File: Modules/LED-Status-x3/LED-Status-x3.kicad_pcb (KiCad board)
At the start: 4 copper layers, 6 parts

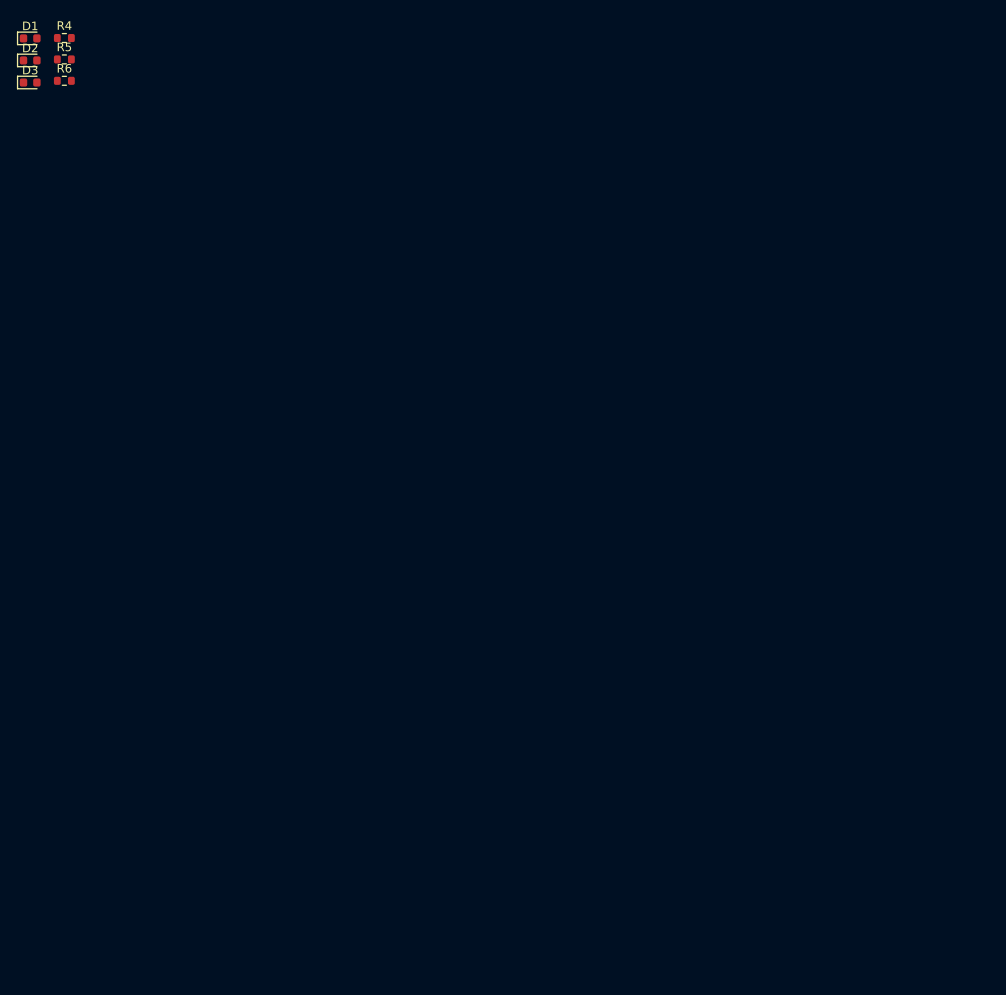
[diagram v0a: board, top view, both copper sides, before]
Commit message: Lay out the LED-Status-x3 module
14 x 11 mm, 4 layers, GND on all four. Three columns at 2.6 mm pitch, LED
above its resistor. Breakout row at y 108.5: two GND vias and the three
LED nets with 1.0 mm stubs on B.Cu. Five F.Fab labels.

DRC: 0 errors, 0 unconnected, 0 parity. The 3 track_dangling warnings are
the 3 interface stubs. Canary 10 to 77.

Co-Authored-By: Claude Opus 5.5 (1M context) <noreply@anthropic.com>
Claude-Session: https://claude.ai/code/session_01ErAAfkmF4h3T5yfrw21utF
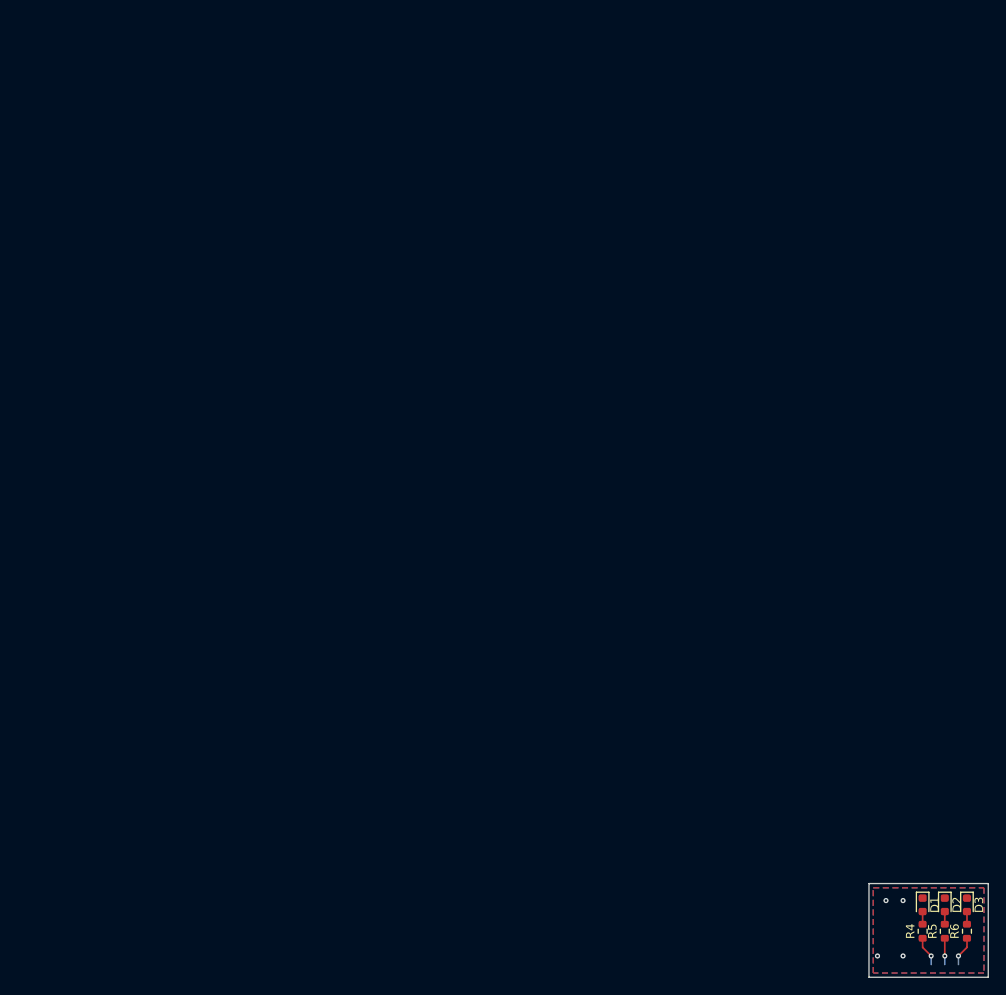
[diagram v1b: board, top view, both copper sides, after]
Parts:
- moved D3 146.3 mm to (111.5, 102.5), turned to -90 degrees
- moved D2 146.1 mm to (108.9, 102.5), turned to -90 degrees
- moved D1 146.0 mm to (106.3, 102.5), turned to -90 degrees
- moved R6 145.6 mm to (111.5, 105.6), turned to 90 degrees
- moved R5 145.4 mm to (108.9, 105.6), turned to 90 degrees
- moved R4 145.4 mm to (106.3, 105.6), turned to 90 degrees
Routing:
- net /LED_RF_TX: track 0.00 -> 3.49 mm, vias 0 -> 1
- net /LED_FAULT: track 0.00 -> 3.49 mm, vias 0 -> 1
- net /LED_LEARN: track 0.00 -> 3.08 mm, vias 0 -> 1
- net Net-(D3-A): track 0.00 -> 1.49 mm
- net Net-(D2-A): track 0.00 -> 1.49 mm
- net Net-(D1-A): track 0.00 -> 1.49 mm
- net GND: vias 0 -> 4
- added copper zone on B.Cu, net GND
- added copper zone on F.Cu, net GND
- added copper zone on In1.Cu, net GND
- added copper zone on In2.Cu, net GND
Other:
- board outline added: 14 x 11 mm
- board text added: "GND"
- board text added: "LED_FAULT"
- board text added: "LED_LEARN"
- board text added: "LED_RF_TX"

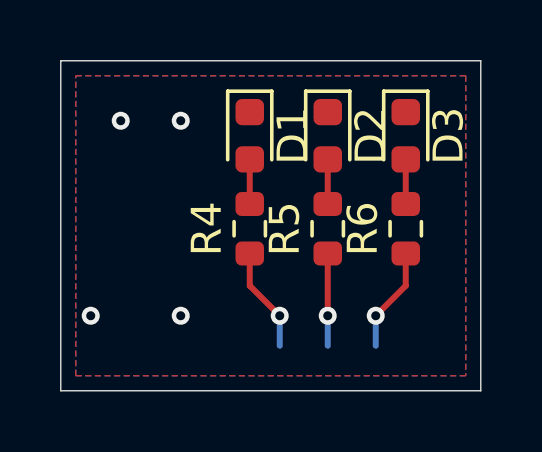
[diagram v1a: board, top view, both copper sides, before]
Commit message: Restore footprints and move passive references to F.Fab
GUI batch 2a on all eight module boards. Update Footprints from Library
restores the (units) blocks that Konnect IPC writes dropped: U10, U1, SW1,
SW2 and U4 no longer report lib_footprint_mismatch. Reference designators of
C, R, L, FB, D, Y and TP parts move to F.Fab. U, J and SW stay on the silk.

Every board: DRC 0 errors, 0 unconnected, 0 parity, the canary fires, and
track_dangling equals the interface stub count.

Co-Authored-By: Claude Opus 5.5 (1M context) <noreply@anthropic.com>
Claude-Session: https://claude.ai/code/session_01ErAAfkmF4h3T5yfrw21utF
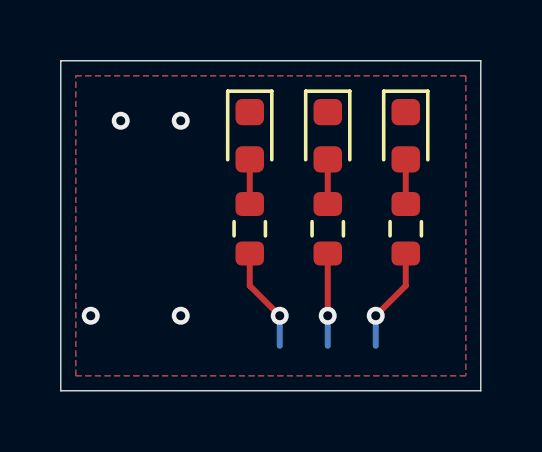
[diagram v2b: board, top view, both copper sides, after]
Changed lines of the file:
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@@
 		(tags "LED")
 		(property "Reference" "D3"
-			(at 0 -1.43 -90)
-			(layer "F.SilkS")
+			(at 0 -1.43 270)
+			(layer "F.Fab")
 			(effects
 				(font
@@
 		)
 		(property "Value" "Red 625nm 0603"
-			(at 0 1.43 -90)
+			(at 0 1.43 270)
 			(layer "F.Fab")
 			(effects
@@
 		)
 		(property "Datasheet" "https://www.we-online.com/components/products/datasheet/150060RS75000.pdf"
-			(at 0 0 -90)
+			(at 0 0 270)
 			(layer "F.Fab")
 			(hide yes)
@@
 		)
 		(property "Description" ""
-			(at 0 0 -90)
+			(at 0 0 270)
 			(layer "F.Fab")
 			(hide yes)
@@
 		)
 		(property "KiLib_Generator" "SMD_2terminal_chip_molded"
-			(at 0 0 -90)
+			(at 0 0 270)
 			(layer "F.SilkS")
 			(hide yes)
@@
 		)
 		(property "MPN" "150060RS75000"
-			(at 0 0 -90)
+			(at 0 0 270)
 			(unlocked yes)
 			(layer "F.Fab")
@@
 		)
 		(property "Manufacturer" "Wurth Elektronik"
-			(at 0 0 -90)
+			(at 0 0 270)
 			(unlocked yes)
 			(layer "F.Fab")
@@
 		)
 		(property "Sim.Pins" "1=K 2=A"
-			(at 0 0 -90)
+			(at 0 0 270)
 			(unlocked yes)
 			(layer "F.Fab")
@@
 		)
 		(fp_text user "${REFERENCE}"
-			(at 0 0 -90)
+			(at 0 0 270)
 			(layer "F.Fab")
 			(effects
@@
 		(property "Reference" "R5"
 			(at 0 -1.43 90)
-			(layer "F.SilkS")
+			(layer "F.Fab")
 			(effects
 				(font
@@
 		(tags "LED")
 		(property "Reference" "D2"
-			(at 0 -1.43 -90)
-			(layer "F.SilkS")
+			(at 0 -1.43 270)
+			(layer "F.Fab")
 			(effects
 				(font
@@
 		)
 		(property "Value" "Amber 605nm 0603"
-			(at 0 1.43 -90)
+			(at 0 1.43 270)
 			(layer "F.Fab")
 			(effects
@@
 		)
 		(property "Datasheet" "https://www.we-online.com/components/products/datasheet/150060AS75000.pdf"
-			(at 0 0 -90)
+			(at 0 0 270)
 			(layer "F.Fab")
 			(hide yes)
@@
 		)
 		(property "Description" ""
-			(at 0 0 -90)
+			(at 0 0 270)
 			(layer "F.Fab")
 			(hide yes)
@@
 		)
 		(property "KiLib_Generator" "SMD_2terminal_chip_molded"
-			(at 0 0 -90)
+			(at 0 0 270)
 			(layer "F.SilkS")
 			(hide yes)
@@
 		)
 		(property "MPN" "150060AS75000"
-			(at 0 0 -90)
+			(at 0 0 270)
 			(unlocked yes)
 			(layer "F.Fab")
@@
 		)
 		(property "Manufacturer" "Wurth Elektronik"
-			(at 0 0 -90)
+			(at 0 0 270)
 			(unlocked yes)
 			(layer "F.Fab")
@@
 		)
 		(property "Sim.Pins" "1=K 2=A"
-			(at 0 0 -90)
+			(at 0 0 270)
 			(unlocked yes)
 			(layer "F.Fab")
@@
 		)
 		(fp_text user "${REFERENCE}"
-			(at 0 0 -90)
+			(at 0 0 270)
 			(layer "F.Fab")
 			(effects
@@
 		(property "Reference" "R4"
 			(at 0 -1.43 90)
-			(layer "F.SilkS")
+			(layer "F.Fab")
 			(effects
 				(font
@@
 		(tags "LED")
 		(property "Reference" "D1"
-			(at 0 -1.43 -90)
-			(layer "F.SilkS")
+			(at 0 -1.43 270)
+			(layer "F.Fab")
 			(effects
 				(font
@@
 		)
 		(property "Value" "Green 570nm 0603"
-			(at 0 1.43 -90)
+			(at 0 1.43 270)
 			(layer "F.Fab")
 			(effects
@@
 		)
 		(property "Datasheet" "https://www.we-online.com/components/products/datasheet/150060VS75000.pdf"
-			(at 0 0 -90)
+			(at 0 0 270)
 			(layer "F.Fab")
 			(hide yes)
@@
 		)
 		(property "Description" ""
-			(at 0 0 -90)
+			(at 0 0 270)
 			(layer "F.Fab")
 			(hide yes)
@@
 		)
 		(property "KiLib_Generator" "SMD_2terminal_chip_molded"
-			(at 0 0 -90)
+			(at 0 0 270)
 			(layer "F.SilkS")
 			(hide yes)
@@
 		)
 		(property "MPN" "150060VS75000"
-			(at 0 0 -90)
+			(at 0 0 270)
 			(unlocked yes)
 			(layer "F.Fab")
@@
 		)
 		(property "Manufacturer" "Wurth Elektronik"
-			(at 0 0 -90)
+			(at 0 0 270)
 			(unlocked yes)
 			(layer "F.Fab")
@@
 		)
 		(property "Sim.Pins" "1=K 2=A"
-			(at 0 0 -90)
+			(at 0 0 270)
 			(unlocked yes)
 			(layer "F.Fab")
@@
 		)
 		(fp_text user "${REFERENCE}"
-			(at 0 0 -90)
+			(at 0 0 270)
 			(layer "F.Fab")
 			(effects
@@
 		(property "Reference" "R6"
 			(at 0 -1.43 90)
-			(layer "F.SilkS")
-			(effects
-				(font
+			(layer "F.Fab")
+			(effects
+				(font
